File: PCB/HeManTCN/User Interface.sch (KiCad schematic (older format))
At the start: 7 parts

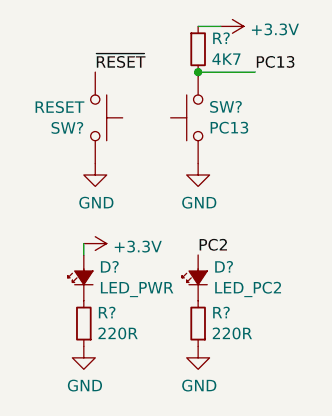
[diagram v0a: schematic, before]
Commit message: Hoja A1
Desarme las hojas jerarquicas y configure la hoja del esquematico como A1. Hay lugar suficiente (por ahora) para todo.
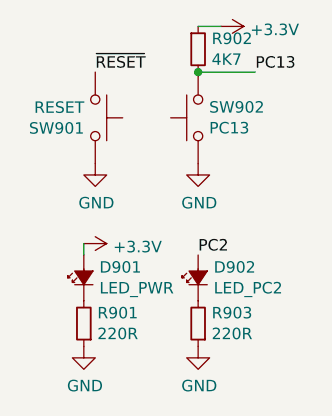
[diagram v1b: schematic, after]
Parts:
- gave numbers to parts that had none: 7
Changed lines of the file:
@@
 $Descr A4 11693 8268
 encoding utf-8
-Sheet 9 11
+Sheet 9 5
 Title "SnifferTCN"
 Date "2019-09-25"
@@
 P 5200 3150
 AR Path="/5DA5F5A5" Ref="SW?"  Part="1"
-AR Path="/5DA5F3DC/5DA5F5A5" Ref="SW?"  Part="1"
-F 0 "SW?" V 5246 3102 50  0000 R CNN
+AR Path="/5DA5F3DC/5DA5F5A5" Ref="SW901"  Part="1"
+F 0 "SW901" V 5246 3102 50  0000 R CNN
 F 1 "RESET" V 5155 3102 50  0000 R CNN
 F 2 "Buttons_Switches_THT:SW_Tactile_SPST_Angled_PTS645Vx31-2LFS" H 5200 3350 50  0001 C CNN
@@
 P 5200 3350
 AR Path="/5DA5F5AC" Ref="#PWR?"  Part="1"
-AR Path="/5DA5F3DC/5DA5F5AC" Ref="#PWR?"  Part="1"
-F 0 "#PWR?" H 5200 3100 50  0001 C CNN
+AR Path="/5DA5F3DC/5DA5F5AC" Ref="#PWR0903"  Part="1"
+F 0 "#PWR0903" H 5200 3100 50  0001 C CNN
 F 1 "GND" H 5205 3177 50  0000 C CNN
 F 2 "" H 5200 3350 50  0001 C CNN
@@
 P 5650 3150
 AR Path="/5DA5F5B4" Ref="SW?"  Part="1"
-AR Path="/5DA5F3DC/5DA5F5B4" Ref="SW?"  Part="1"
-F 0 "SW?" V 5696 3102 50  0000 R CNN
+AR Path="/5DA5F3DC/5DA5F5B4" Ref="SW902"  Part="1"
+F 0 "SW902" V 5696 3102 50  0000 R CNN
 F 1 "PC13" V 5605 3102 50  0000 R CNN
 F 2 "Buttons_Switches_THT:SW_Tactile_SPST_Angled_PTS645Vx31-2LFS" H 5650 3350 50  0001 C CNN
@@
 P 5650 3350
 AR Path="/5DA5F5BB" Ref="#PWR?"  Part="1"
-AR Path="/5DA5F3DC/5DA5F5BB" Ref="#PWR?"  Part="1"
-F 0 "#PWR?" H 5650 3100 50  0001 C CNN
+AR Path="/5DA5F3DC/5DA5F5BB" Ref="#PWR0904"  Part="1"
+F 0 "#PWR0904" H 5650 3100 50  0001 C CNN
 F 1 "GND" H 5655 3177 50  0000 C CNN
 F 2 "" H 5650 3350 50  0001 C CNN
@@
 P 5650 3850
 AR Path="/5DA5F5C3" Ref="D?"  Part="1"
-AR Path="/5DA5F3DC/5DA5F5C3" Ref="D?"  Part="1"
-F 0 "D?" V 5696 3782 50  0000 R CNN
+AR Path="/5DA5F3DC/5DA5F5C3" Ref="D902"  Part="1"
+F 0 "D902" V 5696 3782 50  0000 R CNN
 F 1 "LED_PC2" V 5605 3782 50  0000 R CNN
 F 2 "LED_SMD:LED_0805_2012Metric_Castellated" V 5650 3850 50  0001 C CNN
@@
 P 5650 4050
 AR Path="/5DA5F5CB" Ref="R?"  Part="1"
-AR Path="/5DA5F3DC/5DA5F5CB" Ref="R?"  Part="1"
-F 0 "R?" H 5591 4004 50  0000 R CNN
+AR Path="/5DA5F3DC/5DA5F5CB" Ref="R903"  Part="1"
+F 0 "R903" H 5591 4004 50  0000 R CNN
 F 1 "220R" H 5591 4095 50  0000 R CNN
 F 2 "Resistor_SMD:R_0805_2012Metric" H 5650 4050 50  0001 C CNN
@@
 P 5650 4150
 AR Path="/5DA5F5D2" Ref="#PWR?"  Part="1"
-AR Path="/5DA5F3DC/5DA5F5D2" Ref="#PWR?"  Part="1"
-F 0 "#PWR?" H 5650 3900 50  0001 C CNN
+AR Path="/5DA5F3DC/5DA5F5D2" Ref="#PWR0905"  Part="1"
+F 0 "#PWR0905" H 5650 3900 50  0001 C CNN
 F 1 "GND" H 5655 3977 50  0000 C CNN
 F 2 "" H 5650 4150 50  0001 C CNN
@@
 P 5150 3850
 AR Path="/5DA5F5D9" Ref="D?"  Part="1"
-AR Path="/5DA5F3DC/5DA5F5D9" Ref="D?"  Part="1"
-F 0 "D?" V 5196 3782 50  0000 R CNN
+AR Path="/5DA5F3DC/5DA5F5D9" Ref="D901"  Part="1"
+F 0 "D901" V 5196 3782 50  0000 R CNN
 F 1 "LED_PWR" V 5105 3782 50  0000 R CNN
 F 2 "LED_SMD:LED_0805_2012Metric_Castellated" V 5150 3850 50  0001 C CNN
@@
 P 5150 4050
 AR Path="/5DA5F5E1" Ref="R?"  Part="1"
-AR Path="/5DA5F3DC/5DA5F5E1" Ref="R?"  Part="1"
-F 0 "R?" H 5091 4004 50  0000 R CNN
+AR Path="/5DA5F3DC/5DA5F5E1" Ref="R901"  Part="1"
+F 0 "R901" H 5091 4004 50  0000 R CNN
 F 1 "220R" H 5091 4095 50  0000 R CNN
 F 2 "Resistor_SMD:R_0805_2012Metric" H 5150 4050 50  0001 C CNN
@@
 P 5150 4150
 AR Path="/5DA5F5E8" Ref="#PWR?"  Part="1"
-AR Path="/5DA5F3DC/5DA5F5E8" Ref="#PWR?"  Part="1"
-F 0 "#PWR?" H 5150 3900 50  0001 C CNN
+AR Path="/5DA5F3DC/5DA5F5E8" Ref="#PWR0902"  Part="1"
+F 0 "#PWR0902" H 5150 3900 50  0001 C CNN
 F 1 "GND" H 5155 3977 50  0000 C CNN
 F 2 "" H 5150 4150 50  0001 C CNN
@@
 P 5150 3700
 AR Path="/5DA5F5EE" Ref="#PWR?"  Part="1"
-AR Path="/5DA5F3DC/5DA5F5EE" Ref="#PWR?"  Part="1"
-F 0 "#PWR?" H 5150 3550 50  0001 C CNN
+AR Path="/5DA5F3DC/5DA5F5EE" Ref="#PWR0901"  Part="1"
+F 0 "#PWR0901" H 5150 3550 50  0001 C CNN
 F 1 "+3.3V" V 5165 3828 50  0000 L CNN
 F 2 "" H 5150 3700 50  0001 C CNN
@@
 P 5650 2850
 AR Path="/5DA5F5F6" Ref="R?"  Part="1"
-AR Path="/5DA5F3DC/5DA5F5F6" Ref="R?"  Part="1"
-F 0 "R?" H 5709 2896 50  0000 L CNN
+AR Path="/5DA5F3DC/5DA5F5F6" Ref="R902"  Part="1"
+F 0 "R902" H 5709 2896 50  0000 L CNN
 F 1 "4K7" H 5709 2805 50  0000 L CNN
 F 2 "Resistor_SMD:R_0805_2012Metric" H 5650 2850 50  0001 C CNN
@@
 P 5750 2750
 AR Path="/5DA5F5FF" Ref="#PWR?"  Part="1"
-AR Path="/5DA5F3DC/5DA5F5FF" Ref="#PWR?"  Part="1"
-F 0 "#PWR?" H 5750 2600 50  0001 C CNN
+AR Path="/5DA5F3DC/5DA5F5FF" Ref="#PWR0906"  Part="1"
+F 0 "#PWR0906" H 5750 2600 50  0001 C CNN
 F 1 "+3.3V" V 5765 2878 50  0000 L CNN
 F 2 "" H 5750 2750 50  0001 C CNN
